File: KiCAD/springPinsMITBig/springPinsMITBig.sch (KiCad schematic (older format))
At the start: 21 parts, among them J1 CONN_02X06, J2 CONN_02X06

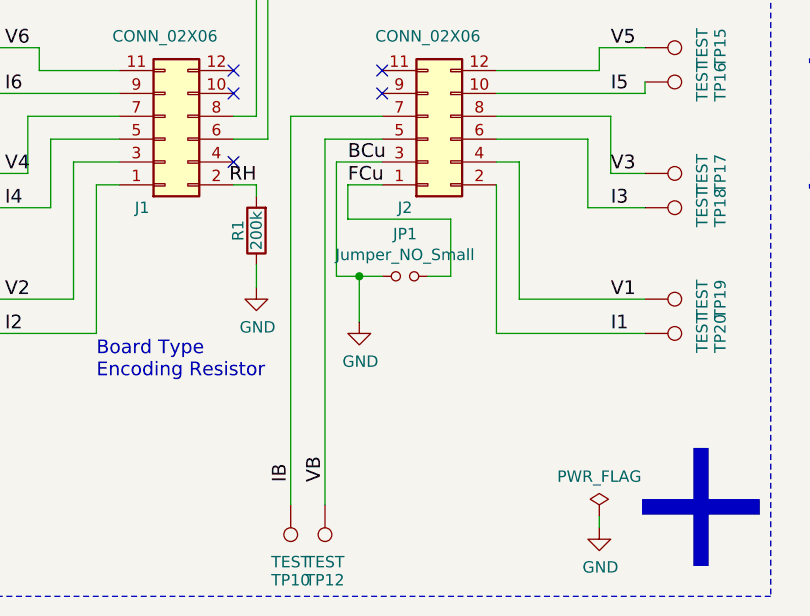
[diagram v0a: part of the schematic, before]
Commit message: clean up mit springpin board names
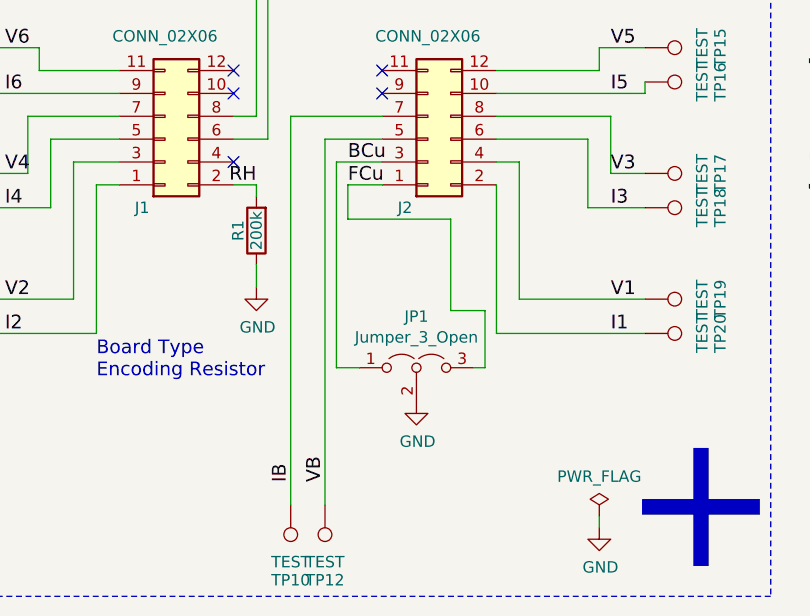
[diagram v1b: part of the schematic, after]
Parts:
- removed JP1: Jumper_NO_Small, Jumper:SolderJumper-2_P1.3mm_Open_RoundedPad1.0x1.5mm, symbol Device:Jumper_NO_Small
- added JP1: Jumper_3_Open, Jumper:SolderJumper-3_P1.3mm_Open_RoundedPad1.0x1.5mm_NumberLabels, symbol Jumper:Jumper_3_Open
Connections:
- net FCu: now also JP1.3 (B)
- net GND: now also JP1.2 (C); no longer J2.3 (Pin_3)
- new net BCu: J2.3 (Pin_3), JP1.1 (A)
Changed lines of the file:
@@
 	1    0    0    -1
 $EndComp
-$Comp
-L Device:Jumper_NO_Small JP1
-U 1 1 59F4B423
-P 5600 4550
-F 0 "JP1" H 5600 4735 50  0000 C CNN
-F 1 "Jumper_NO_Small" H 5600 4644 50  0000 C CNN
-F 2 "Jumper:SolderJumper-2_P1.3mm_Open_RoundedPad1.0x1.5mm" H 5600 4550 50  0001 C CNN
-F 3 "" H 5600 4550 50  0001 C CNN
-	1    5600 4550
-	1    0    0    -1
-$EndComp
-Wire Wire Line
-	5300 4050 5300 4550
-Wire Wire Line
-	5300 4550 5400 4550
 Wire Wire Line
 	5350 4150 5350 4300
 Wire Wire Line
 	5350 4300 5800 4300
-Wire Wire Line
-	5800 4300 5800 4550
-Wire Wire Line
-	5800 4550 5700 4550
 $Comp
 L power:GND #PWR0101
 U 1 1 5C405530
-P 5400 4750
-F 0 "#PWR0101" H 5400 4500 50  0001 C CNN
-F 1 "GND" H 5405 4577 50  0000 C CNN
-F 2 "" H 5400 4750 50  0001 C CNN
-F 3 "" H 5400 4750 50  0001 C CNN
-	1    5400 4750
+P 5650 5100
+F 0 "#PWR0101" H 5650 4850 50  0001 C CNN
+F 1 "GND" H 5655 4927 50  0000 C CNN
+F 2 "" H 5650 5100 50  0001 C CNN
+F 3 "" H 5650 5100 50  0001 C CNN
+	1    5650 5100
 	1    0    0    -1
 $EndComp
-Wire Wire Line
-	5400 4750 5400 4550
-Connection ~ 5400 4550
-Wire Wire Line
-	5400 4550 5500 4550
 NoConn ~ 4850 4050
 Wire Wire Line
@@
 Wire Wire Line
 	6450 5600 6450 5650
+$Comp
+L Jumper:Jumper_3_Open JP1
+U 1 1 5C41BB41
+P 5650 4950
+F 0 "JP1" H 5650 5174 50  0000 C CNN
+F 1 "Jumper_3_Open" H 5650 5083 50  0000 C CNN
+F 2 "Jumper:SolderJumper-3_P1.3mm_Open_RoundedPad1.0x1.5mm_NumberLabels" H 5650 4950 50  0001 C CNN
+F 3 "~" H 5650 4950 50  0001 C CNN
+	1    5650 4950
+	1    0    0    -1
+$EndComp
+Wire Wire Line
+	5400 4950 5300 4950
+Wire Wire Line
+	5300 4050 5300 4950
+Wire Wire Line
+	5800 4700 5950 4700
+Wire Wire Line
+	5950 4700 5950 4950
+Wire Wire Line
+	5950 4950 5900 4950
+Wire Wire Line
+	5800 4300 5800 4700
 $EndSCHEMATC

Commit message: update holder for mit
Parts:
- J1: Farnell code (none) -> 2215306
- J2: farnell code (none) -> 2215306
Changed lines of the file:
@@
 EESchema Schematic File Version 4
-LIBS:springPins30x30NoWindow-cache
+LIBS:springPinsMITBig-cache
 EELAYER 26 0
 EELAYER END
@@
 P 4550 3950
 F 0 "J1" H 4450 4250 50  0000 C CNN
-F 1 "CONN_02X06" H 4550 3500 50  0000 C CNN
+F 1 "CONN_02X06" H 4550 3500 50  0001 C CNN
 F 2 "Connector_PinHeader_2.54mm:PinHeader_2x06_P2.54mm_Vertical" H 4550 2750 50  0001 C CNN
 F 3 "" H 4550 2750 50  0001 C CNN
+F 4 "2215306" H 4550 3950 50  0001 C CNN "Farnell code"
 	1    4550 3950
 	1    0    0    1
@@
 P 5700 3950
 F 0 "J2" H 5600 4250 50  0000 C CNN
-F 1 "CONN_02X06" H 5700 3500 50  0000 C CNN
+F 1 "CONN_02X06" H 5700 3500 50  0001 C CNN
 F 2 "Connector_PinHeader_2.54mm:PinHeader_2x06_P2.54mm_Vertical" H 5700 2750 50  0001 C CNN
-F 3 "" H 5700 2750 50  0001 C CNN
+F 3 "Farnell code" H 5700 2750 50  0001 C CNN
+F 4 "2215306" H 5700 3950 50  0001 C CNN "farnell code"
 	1    5700 3950
 	1    0    0    1

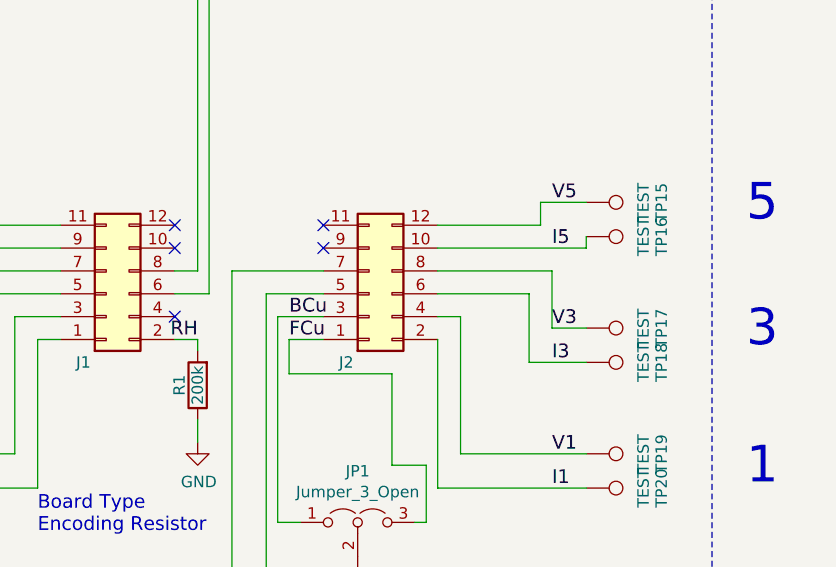
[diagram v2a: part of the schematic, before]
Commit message: update connector components and design printed bottom header shroud
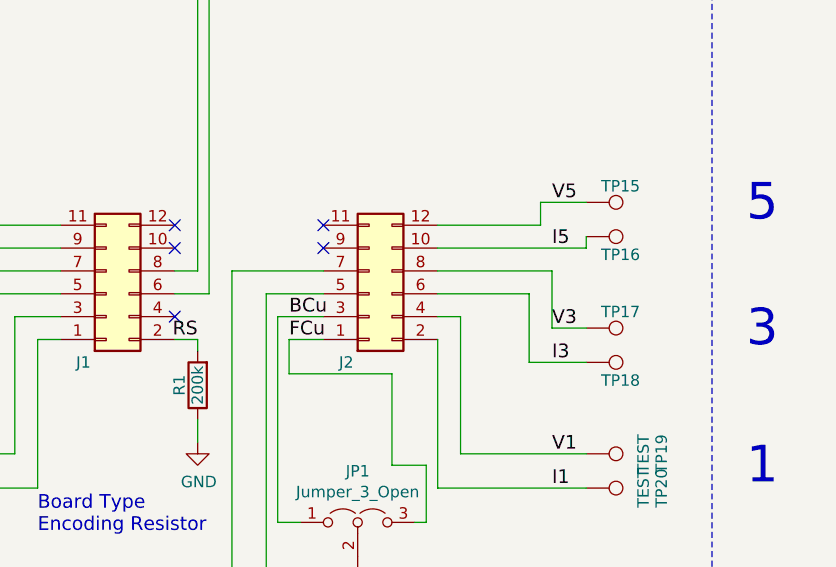
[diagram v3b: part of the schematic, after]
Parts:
- J1: footprint Connector_PinHeader_2.54mm:PinHeader_2x06_P2.54mm_Vertical -> myParts:TSSH-106-01-T-D-04; Farnell code 2215306 -> (none); samtec (none) -> TSSH-106-01-T-D-04
- J2: footprint Connector_PinHeader_2.54mm:PinHeader_2x06_P2.54mm_Vertical -> myParts:TSSH-106-01-T-D; farnell code 2215306 -> (none); samtec (none) -> TSSH-106-01-T-D
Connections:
- net RH renamed RS
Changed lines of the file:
@@
 U 1 1 58E4CA5F
 P 6650 4250
-F 0 "TP18" H 6650 4550 50  0000 C BNN
-F 1 "TEST" H 6650 4500 50  0000 C CNN
+F 0 "TP18" V 6600 4400 50  0000 C BNN
+F 1 "TEST" H 6650 4500 50  0001 C CNN
 F 2 "myParts:S25-022+P25-4023" H 6650 4250 50  0001 C CNN
 F 3 "" H 6650 4250 50  0000 C CNN
@@
 U 1 1 58E4CA65
 P 6650 4100
-F 0 "TP17" H 6650 4400 50  0000 C BNN
-F 1 "TEST" H 6650 4350 50  0000 C CNN
+F 0 "TP17" V 6750 4250 50  0000 C BNN
+F 1 "TEST" H 6650 4350 50  0001 C CNN
 F 2 "myParts:S25-022+P25-4023" H 6650 4100 50  0001 C CNN
 F 3 "" H 6650 4100 50  0000 C CNN
@@
 U 1 1 58E4CA77
 P 6650 3700
-F 0 "TP16" H 6650 4000 50  0000 C BNN
-F 1 "TEST" H 6650 3950 50  0000 C CNN
+F 0 "TP16" V 6600 3850 50  0000 C BNN
+F 1 "TEST" H 6650 3950 50  0001 C CNN
 F 2 "myParts:S25-022+P25-4023" H 6650 3700 50  0001 C CNN
 F 3 "" H 6650 3700 50  0000 C CNN
@@
 U 1 1 58E4CA7D
 P 6650 3550
-F 0 "TP15" H 6650 3850 50  0000 C BNN
-F 1 "TEST" H 6650 3800 50  0000 C CNN
+F 0 "TP15" V 6750 3700 50  0000 C BNN
+F 1 "TEST" H 6650 3800 50  0001 C CNN
 F 2 "myParts:S25-022+P25-4023" H 6650 3550 50  0001 C CNN
 F 3 "" H 6650 3550 50  0000 C CNN
@@
 F 0 "J1" H 4450 4250 50  0000 C CNN
 F 1 "CONN_02X06" H 4550 3500 50  0001 C CNN
-F 2 "Connector_PinHeader_2.54mm:PinHeader_2x06_P2.54mm_Vertical" H 4550 2750 50  0001 C CNN
+F 2 "myParts:TSSH-106-01-T-D-04" H 4550 2750 50  0001 C CNN
 F 3 "" H 4550 2750 50  0001 C CNN
-F 4 "2215306" H 4550 3950 50  0001 C CNN "Farnell code"
+F 4 "TSSH-106-01-T-D-04" H 4550 3950 50  0001 C CNN "samtec"
 	1    4550 3950
 	1    0    0    1
@@
 F 0 "J2" H 5600 4250 50  0000 C CNN
 F 1 "CONN_02X06" H 5700 3500 50  0001 C CNN
-F 2 "Connector_PinHeader_2.54mm:PinHeader_2x06_P2.54mm_Vertical" H 5700 2750 50  0001 C CNN
+F 2 "myParts:TSSH-106-01-T-D" H 5700 2750 50  0001 C CNN
 F 3 "Farnell code" H 5700 2750 50  0001 C CNN
-F 4 "2215306" H 5700 3950 50  0001 C CNN "farnell code"
+F 4 "TSSH-106-01-T-D" H 5700 3950 50  0001 C CNN "samtec"
 	1    5700 3950
 	1    0    0    1
@@
 VB
 Text Label 4950 4150 2    60   ~ 0
-RH
+RS
 Wire Wire Line
 	5350 4150 5500 4150
